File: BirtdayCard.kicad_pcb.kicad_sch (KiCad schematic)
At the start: 31 parts, among them J3 USB_C_Receptacle_USB2.0, Q3 G2312, U1 ESP32-C3-WROOM-02-N4(4MB)

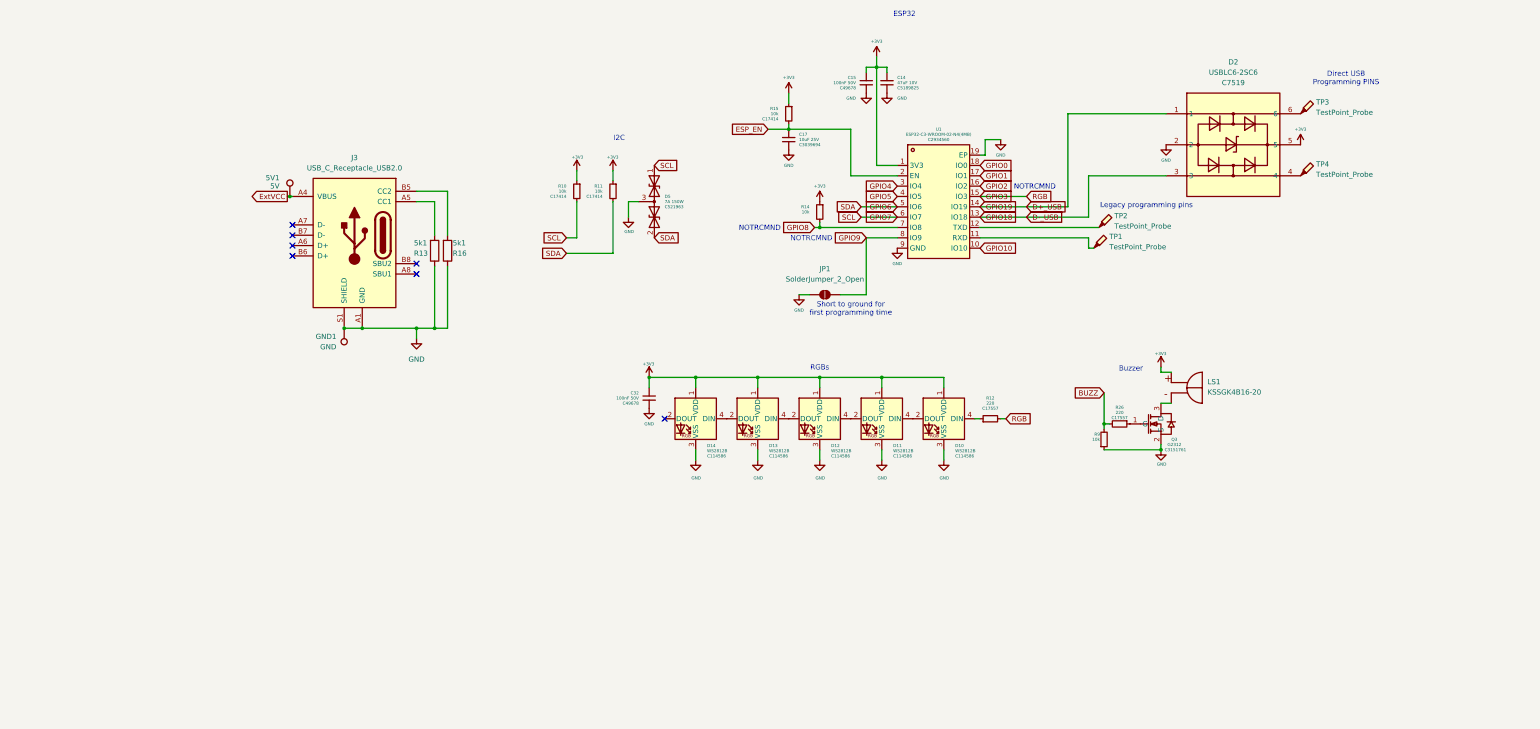
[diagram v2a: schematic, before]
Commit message: USB configured and added LDO
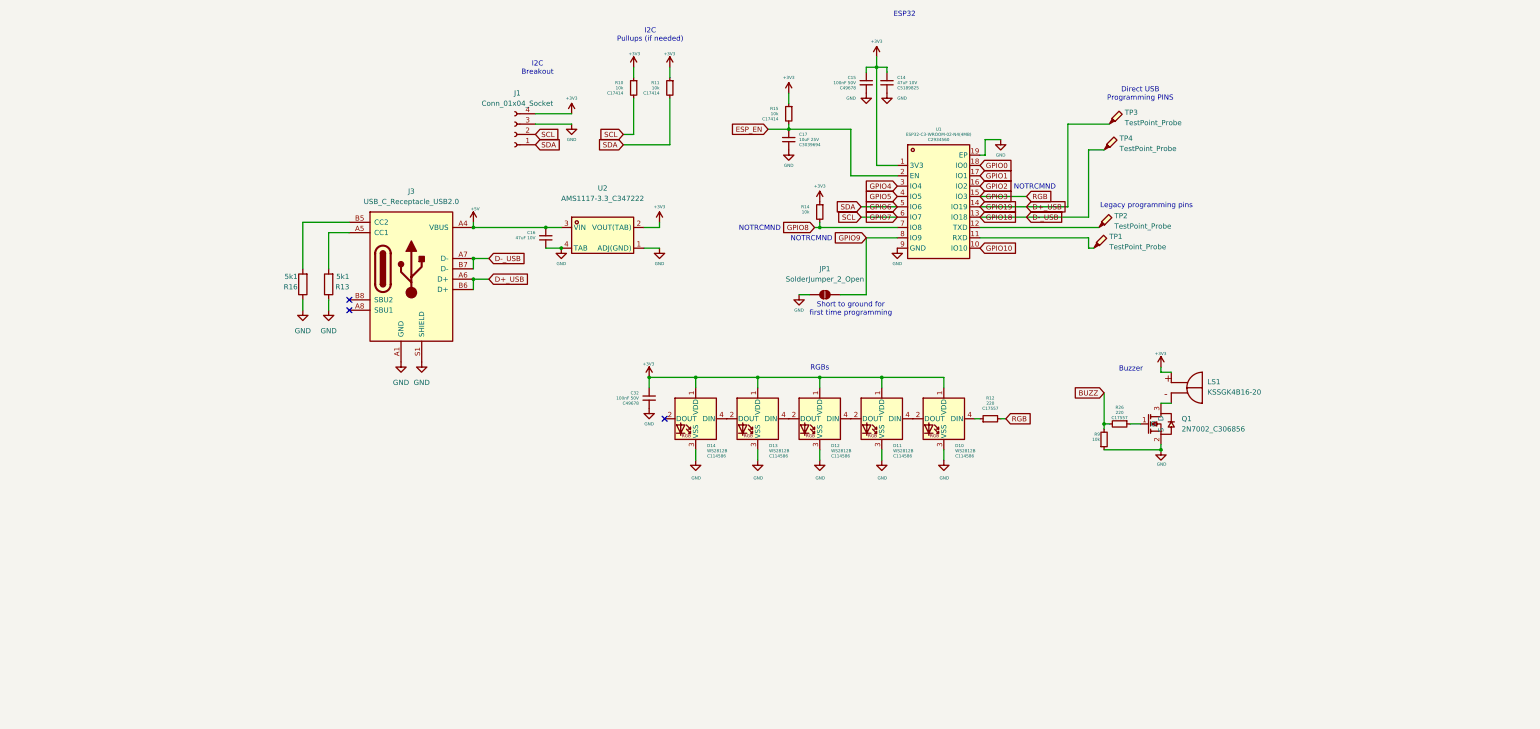
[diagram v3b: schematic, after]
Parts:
- removed 5V1: 5V, TestPoint:TestPoint_Pad_1.0x1.0mm, symbol Connector:TestPoint
- removed D2: USBLC6-2SC6, easyeda2kicad:SOT-23-6_L2.9-W1.6-P0.95-LS2.8-BL, symbol easyeda2kicad:USBLC6-2SC6
- removed D5: 7A 150W, Package_TO_SOT_SMD:SOT-23_Handsoldering, symbol Diode:SM712_SOT23
- removed GND1: GND, TestPoint:TestPoint_Pad_1.0x1.0mm, symbol Connector:TestPoint
- removed Q3: G2312, VolstoraEasyEda:SOT-23_L2.9-W1.3-P1.90-LS2.4-BR, symbol VolstoraEasyEda:G2312
- added C16: 47uF 10V, Capacitor_SMD:C_1210_3225Metric_Pad1.33x2.70mm_HandSolder, symbol Device:C_Small
- added J1: Conn_01x04_Socket, symbol Connector:Conn_01x04_Socket
- added Q1: 2N7002_C306856, easyeda2kicad:SOT-23-3_L2.9-W1.3-P1.90-LS2.4-BR, symbol easyeda2kicad:2N7002_C306856
- added U2: AMS1117-3.3_C347222, easyeda2kicad:SOT-223-4_L6.5-W3.5-P2.30-LS7.0-BR, symbol easyeda2kicad:AMS1117-3.3_C347222
- C15, C17, C32: footprint Capacitor_SMD:C_0805_2012Metric_Pad1.18x1.45mm_HandSolder -> Capacitor_SMD:C_1210_3225Metric_Pad1.33x2.70mm_HandSolder
- D10, D11, D12, D13, D14: footprint VolstoraEasyEda:LED-SMD_4P-L5.0-W5.0-BL_TC5050RGB -> easyeda2kicad:LED-SMD_4P-L5.0-W5.0-BL_TC5050RGB
- JP1: footprint (none) -> Jumper:SolderJumper-2_P1.3mm_Open_Pad1.0x1.5mm
- TP1, TP2, TP3, TP4: footprint (none) -> TestPoint:TestPoint_Pad_D2.0mm
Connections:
- net +3V3: now also J1.4 (Pin_4), U2.2 (VOUT(TAB))
- net D+_USB: now also J3.A6 (D+), J3.B6 (D+), TP3.1
- net D-_USB: now also J3.A7 (D-), J3.B7 (D-), TP4.1
- net GND: now also C16.1, J1.3 (Pin_3), Q1.2 (S), U2.1 (ADJ(GND)), U2.4 (TAB)
- net GPIO6: now also J1.1 (Pin_1)
- net GPIO7: now also J1.2 (Pin_2)
- net at R26.1: now also Q1.1 (G)
- net at LS1.N: now also Q1.3 (D)
- net ExtVCC renamed +5V
- net +5V: now also C16.2, U2.3 (VIN)
- no-connect marks 7 -> 3
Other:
- note added: "I2C Breakout"
- note added: "I2C Pullups (if needed)"
- note added: "Short to ground for first time programming"
- note removed: "I2C"
- note removed: "Short to ground for first programming time"
- moved on the sheet: J3, R10, R11, R13, R16, TP3, TP4

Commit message: General layout improvements, added ESD protection and more LEDS
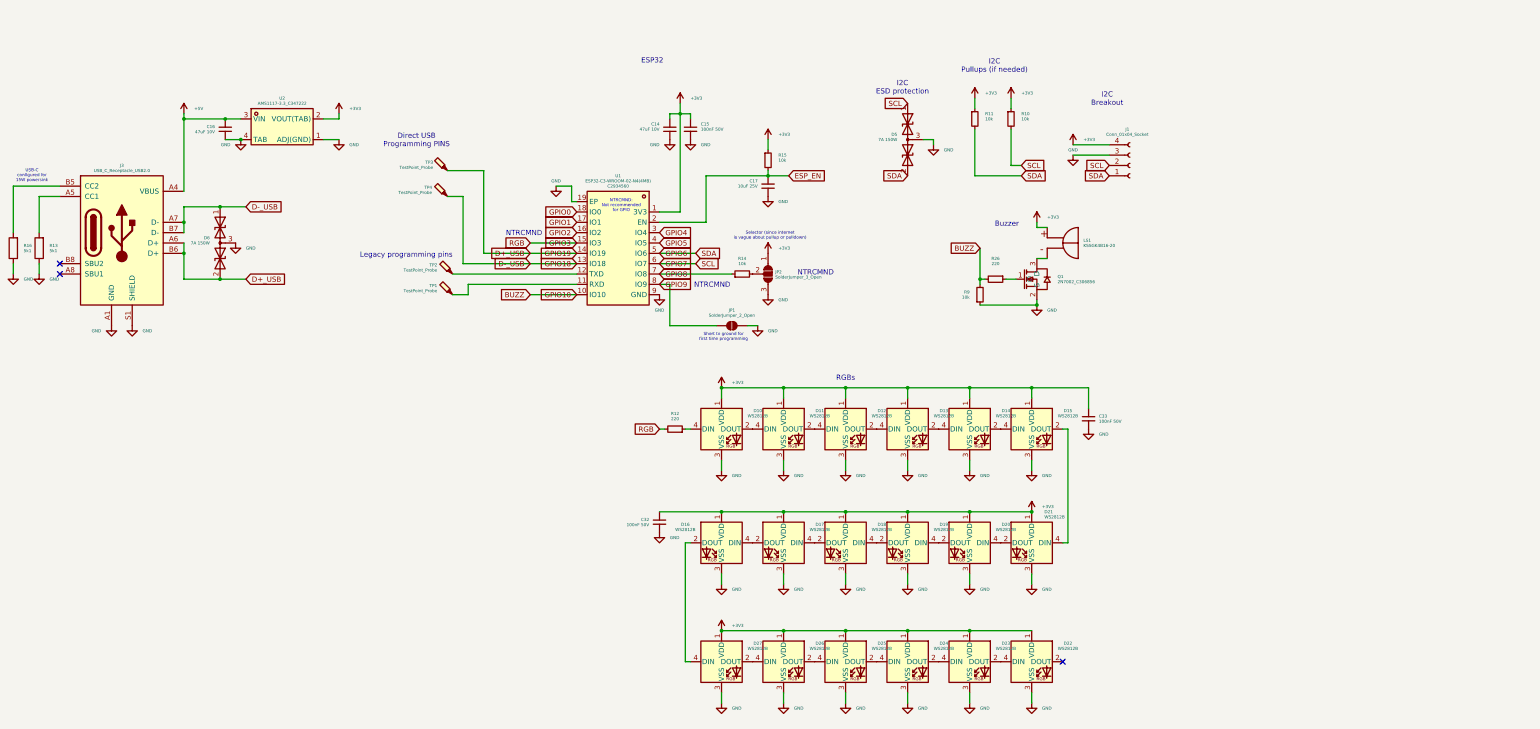
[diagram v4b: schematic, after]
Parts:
- added C33: 100nF 50V, Capacitor_SMD:C_1210_3225Metric_Pad1.33x2.70mm_HandSolder, symbol Device:C_Small
- added D15, D16, D17, D18, D19, D20, D21, D22, D23, D24, D25, D26, D27: WS2812B, easyeda2kicad:LED-SMD_4P-L5.0-W5.0-BL_TC5050RGB, symbol LED:WS2812B
- added D5, D6: 7A 150W, Package_TO_SOT_SMD:SOT-23_Handsoldering, symbol Diode:SM712_SOT23
- added JP2: SolderJumper_3_Open, Jumper:SolderJumper-3_P1.3mm_Open_RoundedPad1.0x1.5mm, symbol Jumper:SolderJumper_3_Open
- J1: footprint (none) -> Connector_PinSocket_2.54mm:PinSocket_1x04_P2.54mm_Vertical
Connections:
- net GPIO10 is gone; now on net BUZZ: U1.10 (IO10)
- net +3V3: now also C33.1, D15.1 (VDD), D16.1 (VDD), D17.1 (VDD), D18.1 (VDD), D19.1 (VDD), D20.1 (VDD), D21.1 (VDD), D22.1 (VDD), D23.1 (VDD), D24.1 (VDD), D25.1 (VDD), D26.1 (VDD), D27.1 (VDD), JP2.1 (A); no longer R14.1
- net D+_USB: now also D6.2 (A2)
- net D-_USB: now also D6.1 (A1)
- net GND: now also C33.2, D15.3 (VSS), D16.3 (VSS), D17.3 (VSS), D18.3 (VSS), D19.3 (VSS), D20.3 (VSS), D21.3 (VSS), D22.3 (VSS), D23.3 (VSS), D24.3 (VSS), D25.3 (VSS), D26.3 (VSS), D27.3 (VSS), D5.3 (common), D6.3 (common), JP2.3 (B)
- net GPIO6: now also D5.2 (A2)
- net GPIO7: now also D5.1 (A1)
- net GPIO8: now also R14.1; no longer R14.2
- net at D14.2 (DOUT): now also D15.4 (DIN)
- new net: D25.4 (DIN), D26.2 (DOUT)
- new net: D26.4 (DIN), D27.2 (DOUT)
- new net: D16.4 (DIN), D17.2 (DOUT)
- new net: D17.4 (DIN), D18.2 (DOUT)
- new net: D16.2 (DOUT), D27.4 (DIN)
- new net: D22.4 (DIN), D23.2 (DOUT)
- new net: JP2.2 (C), R14.2
- new net: D23.4 (DIN), D24.2 (DOUT)
- new net: D24.4 (DIN), D25.2 (DOUT)
- new net: D20.4 (DIN), D21.2 (DOUT)
- new net: D15.2 (DOUT), D21.4 (DIN)
- new net: D18.4 (DIN), D19.2 (DOUT)
- new net: D19.4 (DIN), D20.2 (DOUT)
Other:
- note added: "I2C ESD protection"
- note added: "NTRCMND"
- note added: "NTRCMND: Not recommended for GPIO"
- note added: "Selector (since internet is vague about pullup or pulldown)"
- note added: "USB-C configured for 15W powersink"
- note removed: "NOTRCMND"
- moved on the sheet: C14, C15, C16, C17, C32, D10, D11, D12, D13, D14, J1, J3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

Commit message: archived 3D models
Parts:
- J3: footprint USB-C-Power-tester:TYPE-C-31-M-17_handsolder -> easyeda2kicad:TYPE-C-SMD_TYPE-C-6P_5
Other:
- note added: "POWER IN + USBDATA"
- moved on the sheet: LS1, Q1, R26, R9

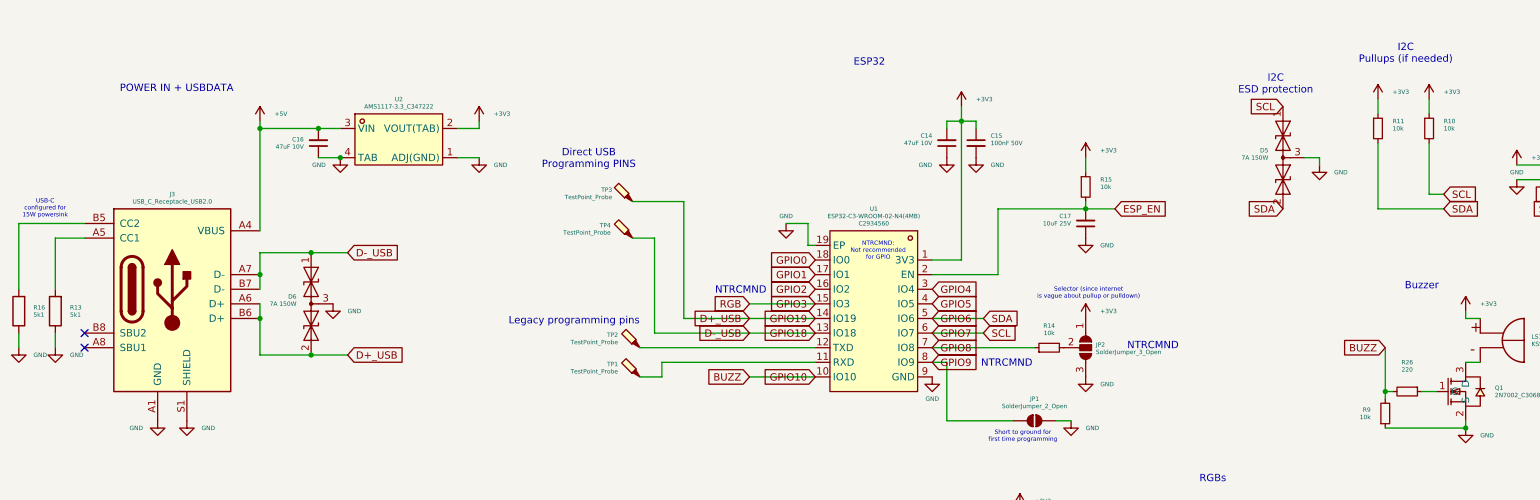
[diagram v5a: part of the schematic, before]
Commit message: added buzzer components and pwr LED
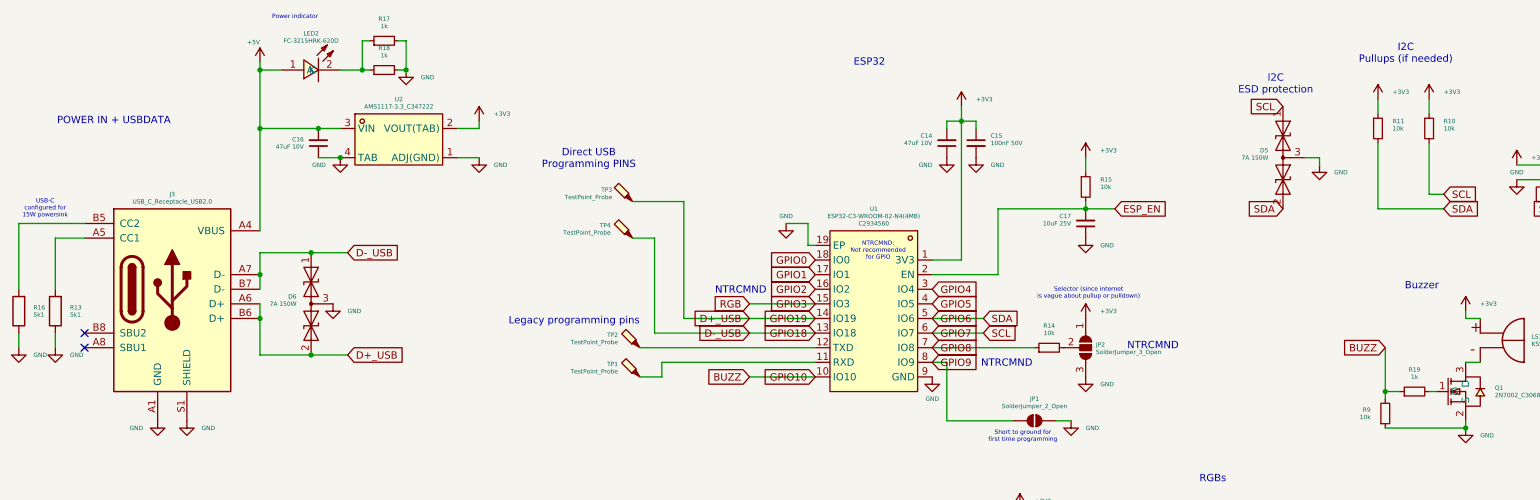
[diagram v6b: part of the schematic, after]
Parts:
- removed R26: 220, Resistor_SMD:R_0805_2012Metric_Pad1.20x1.40mm_HandSolder, symbol Device:R_Small
- added LED2: FC-3215HRK-620D, easyeda2kicad:LED1206-R-RD_RED, symbol easyeda2kicad:FC-3215HRK-620D
- added R17, R18, R19: 1k, Resistor_SMD:R_1206_3216Metric_Pad1.30x1.75mm_HandSolder, symbol Device:R_Small
- LS1: footprint Snapeda:XDCR_KSSGK4B16-20 -> Library:Buzzer KSSGK4B16-20
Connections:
- net +5V: now also LED2.1 (A)
- net BUZZ: now also R19.1
- net GND: now also R17.2, R18.2
- net at Q1.1 (G): now also R19.2
- new net: LED2.2 (K), R17.1, R18.1
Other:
- note added: "Power indicator"

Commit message: Finished V1 of schematic
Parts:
- added KEY1, KEY2: DTSM-61R-V-T/R, easyeda2kicad:KEY-SMD_4P-L6.2-W6.2-P4.50-LS9.0, symbol easyeda2kicad:DTSM-61R-V-T_R
- added TP5, TP6: TestPoint_Probe, TestPoint:TestPoint_Pad_D2.0mm, symbol Connector:TestPoint_Probe
- C14, C16: LCSC Part C5189825 -> (none)
- C15, C32, C33: LCSC Part C49678 -> (none)
- C17: LCSC Part C3039694 -> (none)
- D10, D11, D12, D13, D14, D15, D16, D17, D18, D19, D20, D21, D22, D23, D24, D25, D26, D27: LCSC Part C114586 -> (none)
- D5, D6: LCSC Part C521963 -> (none)
- LED2: LCSC Part C84270 -> (none)
- Q1: LCSC Part C306856 -> (none)
- R10, R11, R14, R15, R17, R18, R19, R9: LCSC Part C17414 -> (none)
- R12: LCSC Part C17557 -> (none)
- U1: LCSC Part C2934560 -> (none)
- U2: LCSC Part C347222 -> (none)
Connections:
- net GND: now also KEY1.1, KEY1.2, KEY2.1, KEY2.2
- net GPIO0: now also TP5.1
- net GPIO1: now also TP6.1
- net GPIO4: now also KEY2.3, KEY2.4
- net GPIO5: now also KEY1.3, KEY1.4
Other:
- moved on the sheet: C14, C15, C16, C17, JP2, R14, R15, U2

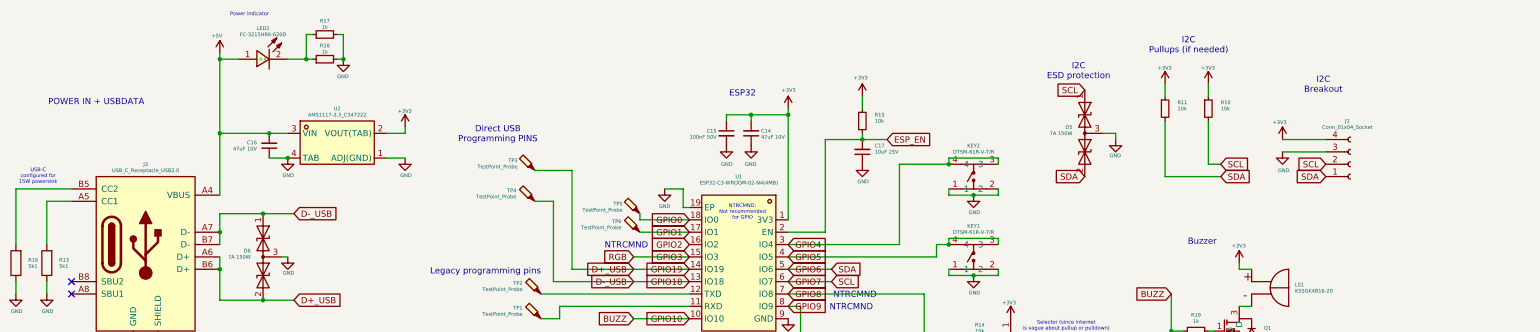
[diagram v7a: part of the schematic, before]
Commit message: Enlarged PCB and working on text
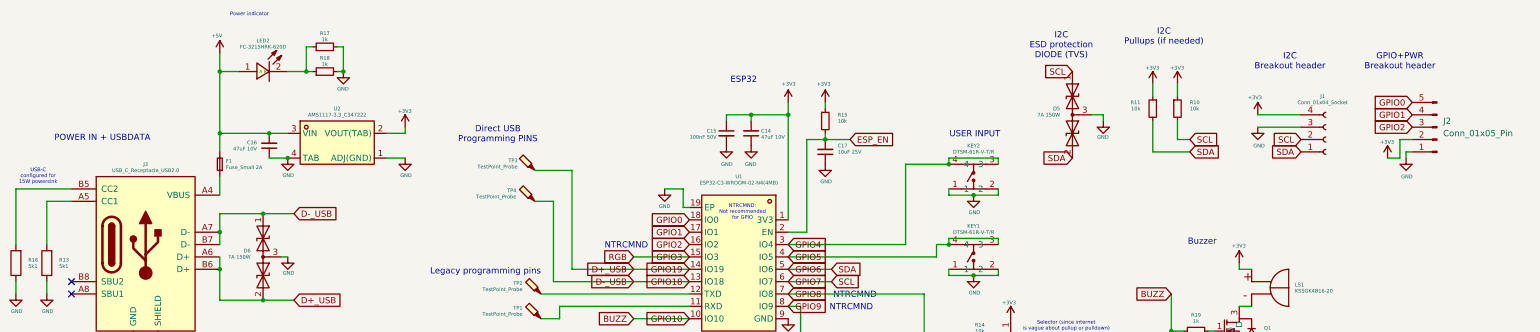
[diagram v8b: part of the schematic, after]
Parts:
- removed TP5, TP6: TestPoint_Probe, TestPoint:TestPoint_Pad_D2.0mm, symbol Connector:TestPoint_Probe
- added F1: Fuse_Small 2A, Fuse:Fuse_1206_3216Metric_Pad1.42x1.75mm_HandSolder, symbol Device:Fuse_Small
- added J2: Conn_01x05_Pin, symbol Connector:Conn_01x05_Pin
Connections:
- net +3V3: now also J2.2 (Pin_2)
- net +5V: now also F1.2; no longer J3.A4 (VBUS), J3.A9 (VBUS), J3.B4 (VBUS), J3.B9 (VBUS)
- net GND: now also J2.1 (Pin_1)
- net GPIO0: now also J2.5 (Pin_5)
- net GPIO1: now also J2.4 (Pin_4)
- net GPIO2: now also J2.3 (Pin_3)
- new net: F1.1, J3.A4 (VBUS), J3.A9 (VBUS), J3.B4 (VBUS), J3.B9 (VBUS)
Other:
- note added: "GPIO+PWR Breakout header"
- note added: "I2C Breakout header"
- note added: "I2C ESD protection DIODE (TVS)"
- note added: "USER INPUT"
- note removed: "I2C Breakout"
- note removed: "I2C ESD protection"
- moved on the sheet: C17, D5, J1, LED2, R10, R11, R15, R17, R18
